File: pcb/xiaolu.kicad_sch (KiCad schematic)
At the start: 35 parts, among them J1 Conn_01x04_Male, J2 AudioJack4, SW1 SW_Push, SW10 SW_Push, SW11 SW_Push, SW12 SW_Push, SW13 SW_Push, SW14 SW_Push, SW15 SW_Push, SW16 SW_Push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

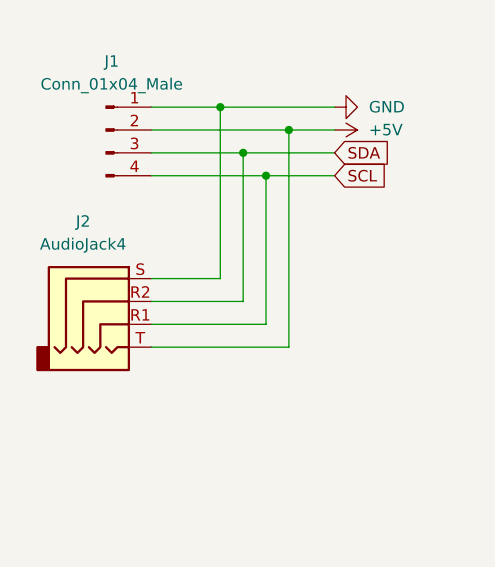
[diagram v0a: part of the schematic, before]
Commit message: fix TRRS symbol
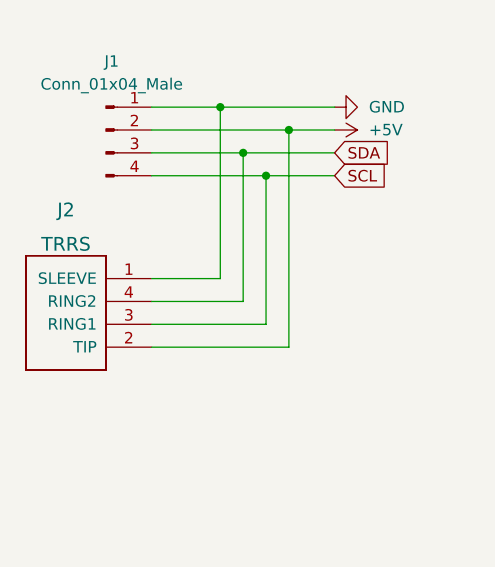
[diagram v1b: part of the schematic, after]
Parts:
- J2: value AudioJack4 -> TRRS; symbol Connector:AudioJack4 -> keebio:TRRS
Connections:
- net +5V: now also J2.2 (TIP); no longer J2.T
- net GND: now also J2.1 (SLEEVE); no longer J2.S
- net SCL: now also J2.3 (RING1); no longer J2.R1
- net SDA: now also J2.4 (RING2); no longer J2.R2
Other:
- moved on the sheet: J2
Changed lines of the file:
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@@
     (pin "1")
   )
-  (symbol (lib_id "Connector:AudioJack4") (at 63.5 132.08 0) (unit 1)
-    (in_bom yes) (on_board yes) (fields_autoplaced)
-    (property "Reference" "J2" (id 0) (at 60.96 123.19 0))
-    (property "Value" "AudioJack4" (id 1) (at 60.96 125.73 0))
-    (property "Footprint" "Xiaolu-Specific:TRRS-PJ-320A" (id 2) (at 63.5 132.08 0)
-      (effects (font (size 1.27 1.27)) hide)
-    )
-    (property "Datasheet" "~" (id 3) (at 63.5 132.08 0)
-      (effects (font (size 1.27 1.27)) hide)
-    )
-    (pin "R1")
-    (pin "R2")
-    (pin "S")
-    (pin "T")
+  (symbol (lib_id "keebio:TRRS") (at 59.69 127 180) (unit 1)
+    (in_bom yes) (on_board yes) (fields_autoplaced)
+    (property "Reference" "J2" (id 0) (at 59.055 121.92 0)
+      (effects (font (size 1.524 1.524)))
+    )
+    (property "Value" "TRRS" (id 1) (at 59.055 125.73 0)
+      (effects (font (size 1.524 1.524)))
+    )
+    (property "Footprint" "Xiaolu-Specific:TRRS-PJ-320A" (id 2) (at 55.88 127 0)
+      (effects (font (size 1.524 1.524)) hide)
+    )
+    (property "Datasheet" "~" (id 3) (at 55.88 127 0)
+      (effects (font (size 1.524 1.524)) hide)
+    )
+    (pin "1")
+    (pin "2")
+    (pin "3")
+    (pin "4")
   )
   (symbol (lib_id "Device:D_Small") (at 236.22 59.69 90) (unit 1)
@@
     )
     (path "/75c6c114-4c92-4cd3-b594-b71491cab033"
-      (reference "J2") (unit 1) (value "AudioJack4") (footprint "Xiaolu-Specific:TRRS-PJ-320A")
+      (reference "J2") (unit 1) (value "TRRS") (footprint "Xiaolu-Specific:TRRS-PJ-320A")
     )
     (path "/a7ae1a4c-2b24-4280-96fc-27eb49b6c4a7"

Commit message: replace XIAO footprint with XIAO-Generic-Hybrid-14P-2.54-21X17.8MM
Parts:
- U1: footprint Xiaolu-Specific:XIAO-SAMD21-RP2040-Hybrid-14P-2.54-21X17.8MM -> Xiaolu-Specific:XIAO-Generic-Hybrid-14P-2.54-21X17.8MM
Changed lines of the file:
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@@
       (effects (font (size 1.27 1.27)) (justify left))
     )
-    (property "Footprint" "Xiaolu-Specific:XIAO-SAMD21-RP2040-Hybrid-14P-2.54-21X17.8MM" (id 2) (at 74.93 49.53 0)
+    (property "Footprint" "Xiaolu-Specific:XIAO-Generic-Hybrid-14P-2.54-21X17.8MM" (id 2) (at 74.93 49.53 0)
       (effects (font (size 1.27 1.27)) hide)
     )
@@
     )
     (path "/31979451-8777-4b8b-b45d-fef92cd05572"
-      (reference "U1") (unit 1) (value "Seeed Studio XIAO SAMD21") (footprint "Xiaolu-Specific:XIAO-SAMD21-RP2040-Hybrid-14P-2.54-21X17.8MM")
-    )
-  )
+      (reference "U1") (unit 1) (value "Seeed Studio XIAO SAMD21") (footprint "Xiaolu-Specific:XIAO-Generic-Hybrid-14P-2.54-21X17.8MM")
+    )
+  )

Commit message: fix Grove connector
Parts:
- J1: footprint Xiaolu-Specific:NS-Tech_Grove_1x04_P2mm_Horizontal -> Connector:NS-Tech_Grove_1x04_P2mm_Vertical
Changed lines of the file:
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@@
     (property "Reference" "J1" (id 0) (at 64.135 105.41 0))
     (property "Value" "Conn_01x04_Male" (id 1) (at 64.135 107.95 0))
-    (property "Footprint" "Xiaolu-Specific:NS-Tech_Grove_1x04_P2mm_Horizontal" (id 2) (at 63.5 113.03 0)
+    (property "Footprint" "Connector:NS-Tech_Grove_1x04_P2mm_Vertical" (id 2) (at 63.5 113.03 0)
       (effects (font (size 1.27 1.27)) hide)
     )
@@
     )
     (path "/b1765cdf-6a38-4dd8-bdad-abffed91abd0"
-      (reference "J1") (unit 1) (value "Conn_01x04_Male") (footprint "Xiaolu-Specific:NS-Tech_Grove_1x04_P2mm_Horizontal")
+      (reference "J1") (unit 1) (value "Conn_01x04_Male") (footprint "Connector:NS-Tech_Grove_1x04_P2mm_Vertical")
     )
     (path "/75c6c114-4c92-4cd3-b594-b71491cab033"

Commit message: use NS-Tech_Grove_1x04_P2mm_Hybrid.kicad_mod for grove connector footprint and fix the Grove connector position
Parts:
- J1: footprint Connector:NS-Tech_Grove_1x04_P2mm_Vertical -> Xiaolu-Specific:NS-Tech_Grove_1x04_P2mm_Hybrid
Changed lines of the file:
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@@
     (property "Reference" "J1" (id 0) (at 64.135 105.41 0))
     (property "Value" "Conn_01x04_Male" (id 1) (at 64.135 107.95 0))
-    (property "Footprint" "Connector:NS-Tech_Grove_1x04_P2mm_Vertical" (id 2) (at 63.5 113.03 0)
+    (property "Footprint" "Xiaolu-Specific:NS-Tech_Grove_1x04_P2mm_Hybrid" (id 2) (at 63.5 113.03 0)
       (effects (font (size 1.27 1.27)) hide)
     )
@@
     )
     (path "/b1765cdf-6a38-4dd8-bdad-abffed91abd0"
-      (reference "J1") (unit 1) (value "Conn_01x04_Male") (footprint "Connector:NS-Tech_Grove_1x04_P2mm_Vertical")
+      (reference "J1") (unit 1) (value "Conn_01x04_Male") (footprint "Xiaolu-Specific:NS-Tech_Grove_1x04_P2mm_Hybrid")
     )
     (path "/75c6c114-4c92-4cd3-b594-b71491cab033"

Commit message: Assign "LCSC Part #" of diodes (D1....D16) to C2128 (1N4148WS)
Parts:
- D1, D11, D12, D14, D2, D3, D5, D7, D8, D9, SW10, SW13, SW14, SW16, SW4, SW8, SW9: LCSC Part # (none) -> C2128
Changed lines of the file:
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@@
+      (effects (font (size 1.27 1.27)) hide)
+    )
+    (property "LCSC Part #" "C2128" (id 4) (at 261.62 85.09 90)
       (effects (font (size 1.27 1.27)) hide)
     )
@@
       (effects (font (size 1.27 1.27)) hide)
     )
+    (property "LCSC Part #" "C2128" (id 4) (at 185.42 85.09 90)
+      (effects (font (size 1.27 1.27)) hide)
+    )
     (pin "1")
     (pin "2")
@@
     )
     (property "Datasheet" "" (id 3) (at 160.02 180.34 0)
+      (effects (font (size 1.27 1.27)) hide)
+    )
+    (property "LCSC Part #" "C2128" (id 4) (at 160.02 180.34 0)
       (effects (font (size 1.27 1.27)) hide)
     )
@@
       (effects (font (size 1.27 1.27)) hide)
     )
+    (property "LCSC Part #" "C2128" (id 4) (at 177.8 120.65 0)
+      (effects (font (size 1.27 1.27)) hide)
+    )
     (pin "1")
     (pin "2")
@@
     )
     (property "Datasheet" "~" (id 3) (at 228.6 44.45 0)
+      (effects (font (size 1.27 1.27)) hide)
+    )
+    (property "LCSC Part #" "C2128" (id 4) (at 228.6 44.45 0)
       (effects (font (size 1.27 1.27)) hide)
     )
@@
       (effects (font (size 1.27 1.27)) hide)
     )
+    (property "LCSC Part #" "C2128" (id 4) (at 210.82 135.89 90)
+      (effects (font (size 1.27 1.27)) hide)
+    )
     (pin "1")
     (pin "2")
@@
       (effects (font (size 1.27 1.27)) hide)
     )
+    (property "LCSC Part #" "C2128" (id 4) (at 160.02 187.96 0)
+      (effects (font (size 1.27 1.27)) hide)
+    )
     (pin "1")
   )
@@
       (effects (font (size 1.27 1.27)) hide)
     )
+    (property "LCSC Part #" "C2128" (id 4) (at 236.22 110.49 90)
+      (effects (font (size 1.27 1.27)) hide)
+    )
     (pin "1")
     (pin "2")
@@
     )
     (property "Datasheet" "" (id 3) (at 160.02 172.72 0)
+      (effects (font (size 1.27 1.27)) hide)
+    )
+    (property "LCSC Part #" "C2128" (id 4) (at 160.02 172.72 0)
       (effects (font (size 1.27 1.27)) hide)
     )
@@
       (effects (font (size 1.27 1.27)) hide)
     )
+    (property "LCSC Part #" "C2128" (id 4) (at 160.02 172.72 0)
+      (effects (font (size 1.27 1.27)) hide)
+    )
     (pin "1")
   )
@@
     )
     (property "Datasheet" "~" (id 3) (at 236.22 59.69 90)
+      (effects (font (size 1.27 1.27)) hide)
+    )
+    (property "LCSC Part #" "C2128" (id 4) (at 236.22 59.69 90)
       (effects (font (size 1.27 1.27)) hide)
     )
@@
       (effects (font (size 1.27 1.27)) hide)
     )
+    (property "LCSC Part #" "C2128" (id 4) (at 254 44.45 0)
+      (effects (font (size 1.27 1.27)) hide)
+    )
     (pin "1")
     (pin "2")
@@
     )
     (property "Datasheet" "" (id 3) (at 86.36 76.2 0)
+      (effects (font (size 1.27 1.27)) hide)
+    )
+    (property "LCSC Part #" "C2128" (id 4) (at 86.36 76.2 0)
       (effects (font (size 1.27 1.27)) hide)
     )
@@
       (effects (font (size 1.27 1.27)) hide)
     )
+    (property "LCSC Part #" "C2128" (id 4) (at 254 120.65 0)
+      (effects (font (size 1.27 1.27)) hide)
+    )
     (pin "1")
     (pin "2")
@@
       (effects (font (size 1.27 1.27)) hide)
     )
+    (property "LCSC Part #" "C2128" (id 4) (at 203.2 120.65 0)
+      (effects (font (size 1.27 1.27)) hide)
+    )
     (pin "1")
     (pin "2")
@@
       (effects (font (size 1.27 1.27)) hide)
     )
+    (property "LCSC Part #" "C2128" (id 4) (at 210.82 110.49 90)
+      (effects (font (size 1.27 1.27)) hide)
+    )
     (pin "1")
     (pin "2")
@@
       (effects (font (size 1.27 1.27)) hide)
     )
+    (property "LCSC Part #" "C2128" (id 4) (at 185.42 59.69 90)
+      (effects (font (size 1.27 1.27)) hide)
+    )
     (pin "1")
     (pin "2")
@@
     )
     (property "Datasheet" "~" (id 3) (at 210.82 59.69 90)
+      (effects (font (size 1.27 1.27)) hide)
+    )
+    (property "LCSC Part #" "C2128" (id 4) (at 210.82 59.69 90)
       (effects (font (size 1.27 1.27)) hide)
     )
@@
       (effects (font (size 1.27 1.27)) hide)
     )
+    (property "LCSC Part #" "C2128" (id 4) (at 254 69.85 0)
+      (effects (font (size 1.27 1.27)) hide)
+    )
     (pin "1")
     (pin "2")
@@
     )
     (property "Datasheet" "" (id 3) (at 88.9 113.03 0)
+      (effects (font (size 1.27 1.27)) hide)
+    )
+    (property "LCSC Part #" "C2128" (id 4) (at 88.9 113.03 0)
       (effects (font (size 1.27 1.27)) hide)
     )
@@
       (effects (font (size 1.27 1.27)) hide)
     )
+    (property "LCSC Part #" "C2128" (id 4) (at 185.42 110.49 90)
+      (effects (font (size 1.27 1.27)) hide)
+    )
     (pin "1")
     (pin "2")
@@
       (effects (font (size 1.27 1.27)) hide)
     )
+    (property "LCSC Part #" "C2128" (id 4) (at 236.22 135.89 90)
+      (effects (font (size 1.27 1.27)) hide)
+    )
     (pin "1")
     (pin "2")
@@
       (effects (font (size 1.27 1.27)) hide)
     )
+    (property "LCSC Part #" "C2128" (id 4) (at 228.6 69.85 0)
+      (effects (font (size 1.27 1.27)) hide)
+    )

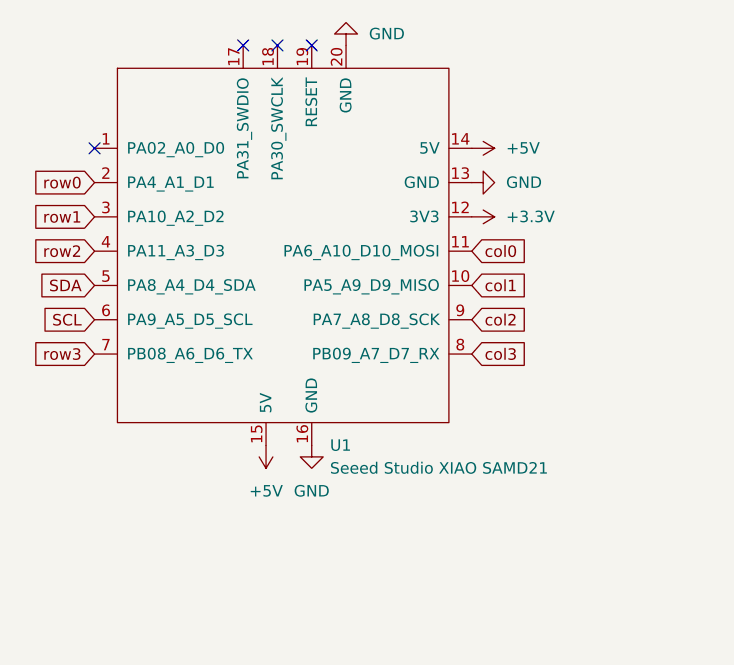
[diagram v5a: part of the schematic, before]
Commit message: flag unconnected to unused pads of xiao
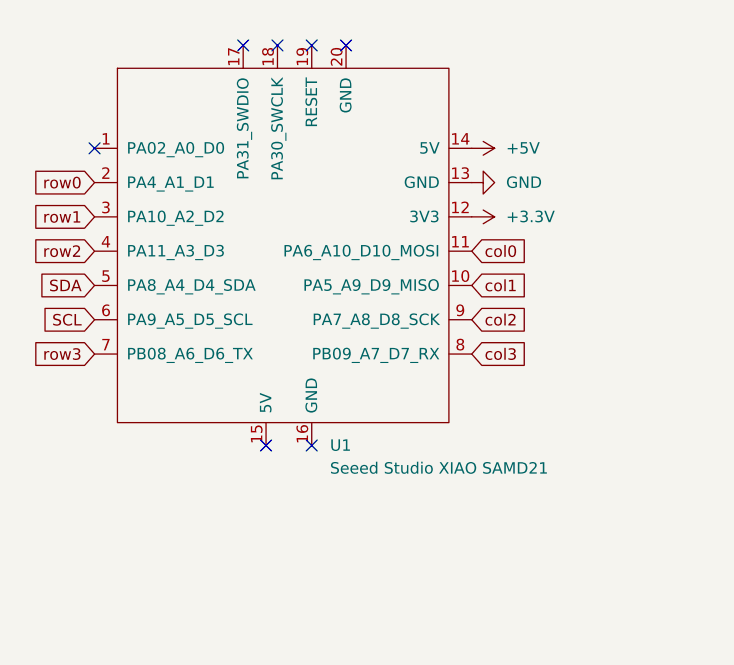
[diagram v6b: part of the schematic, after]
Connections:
- net +5V: no longer U1.15 (5V)
- net GND: no longer U1.16 (GND), U1.20 (GND)
- no-connect marks 4 -> 7
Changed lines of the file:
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@@
   (no_connect (at 78.74 31.75))
   (no_connect (at 86.36 31.75))
+  (no_connect (at 81.28 76.2))
+  (no_connect (at 86.36 76.2))
   (no_connect (at 62.23 43.18))
   (no_connect (at 82.55 31.75))
+  (no_connect (at 90.17 31.75))
   (wire (pts (xy 236.22 125.73) (xy 233.68 125.73))
     (stroke (width 0) (type default) (color 0 0 0 0))
@@
     )
     (property "Datasheet" "" (id 3) (at 104.14 43.18 0)
-      (effects (font (size 1.27 1.27)) hide)
-    )
-    (pin "1")
-  )
-  (symbol (lib_id "power:GND") (at 90.17 31.75 180) (unit 1)
-    (in_bom yes) (on_board yes) (fields_autoplaced)
-    (property "Reference" "#PWR05" (id 0) (at 90.17 25.4 0)
-      (effects (font (size 1.27 1.27)) hide)
-    )
-    (property "Value" "GND" (id 1) (at 92.71 30.4799 0)
-      (effects (font (size 1.27 1.27)) (justify right))
-    )
-    (property "Footprint" "" (id 2) (at 90.17 31.75 0)
-      (effects (font (size 1.27 1.27)) hide)
-    )
-    (property "Datasheet" "" (id 3) (at 90.17 31.75 0)
       (effects (font (size 1.27 1.27)) hide)
     )
@@
     (pin "2")
   )
-  (symbol (lib_id "power:+5V") (at 81.28 76.2 180) (unit 1)
-    (in_bom yes) (on_board yes) (fields_autoplaced)
-    (property "Reference" "#PWR03" (id 0) (at 81.28 72.39 0)
-      (effects (font (size 1.27 1.27)) hide)
-    )
-    (property "Value" "+5V" (id 1) (at 81.28 81.28 0))
-    (property "Footprint" "" (id 2) (at 81.28 76.2 0)
-      (effects (font (size 1.27 1.27)) hide)
-    )
-    (property "Datasheet" "" (id 3) (at 81.28 76.2 0)
-      (effects (font (size 1.27 1.27)) hide)
-    )
-    (pin "1")
-  )
   (symbol (lib_id "power:+3.3V") (at 160.02 187.96 270) (unit 1)
     (in_bom yes) (on_board yes) (fields_autoplaced)
@@
     (pin "2")
   )
-  (symbol (lib_id "power:GND") (at 86.36 76.2 0) (unit 1)
-    (in_bom yes) (on_board yes) (fields_autoplaced)
-    (property "Reference" "#PWR04" (id 0) (at 86.36 82.55 0)
-      (effects (font (size 1.27 1.27)) hide)
-    )
-    (property "Value" "GND" (id 1) (at 86.36 81.28 0))
-    (property "Footprint" "" (id 2) (at 86.36 76.2 0)
-      (effects (font (size 1.27 1.27)) hide)
-    )
-    (property "Datasheet" "" (id 3) (at 86.36 76.2 0)
-      (effects (font (size 1.27 1.27)) hide)
-    )
-    (property "LCSC Part #" "C2128" (id 4) (at 86.36 76.2 0)
-      (effects (font (size 1.27 1.27)) hide)
-    )
-    (pin "1")
-  )
   (symbol (lib_id "power:PWR_FLAG") (at 160.02 180.34 90) (unit 1)
     (in_bom yes) (on_board yes) (fields_autoplaced)
@@
       (reference "#PWR02") (unit 1) (value "+5V") (footprint "")
     )
-    (path "/3553bc35-9f95-4817-85a7-17e531db1a71"
-      (reference "#PWR03") (unit 1) (value "+5V") (footprint "")
-    )
-    (path "/8adb19c1-6f4e-4373-9001-846d6097e7f5"
-      (reference "#PWR04") (unit 1) (value "GND") (footprint "")
-    )
-    (path "/0cd8ac2f-d4e5-49d7-95f0-562595e83db6"
-      (reference "#PWR05") (unit 1) (value "GND") (footprint "")
-    )
     (path "/0b31afd7-5fe7-4ed2-8f8a-50ac88bd6e7e"

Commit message: fix "LCSC Part #"
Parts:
- D10, D13, D15, D16, D4, D6: LCSC Part # (none) -> C2128
- SW10, SW13, SW14, SW16, SW4, SW8, SW9: LCSC Part # C2128 -> (none)
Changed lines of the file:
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@@
       (effects (font (size 1.27 1.27)) hide)
     )
-    (property "LCSC Part #" "C2128" (id 4) (at 261.62 85.09 90)
+    (property "LCSC Part #" "C2128" (id 3) (at 261.62 85.09 90)
       (effects (font (size 1.27 1.27)) hide)
     )
@@
       (effects (font (size 1.27 1.27)) hide)
     )
+    (property "LCSC Part #" "C2128" (id 3) (at 185.42 135.89 90)
+      (effects (font (size 1.27 1.27)) hide)
+    )
     (pin "1")
     (pin "2")
@@
       (effects (font (size 1.27 1.27)) hide)
     )
-    (property "LCSC Part #" "C2128" (id 4) (at 185.42 85.09 90)
+    (property "LCSC Part #" "C2128" (id 3) (at 185.42 85.09 90)
       (effects (font (size 1.27 1.27)) hide)
     )
@@
       (effects (font (size 1.27 1.27)) hide)
     )
+    (property "LCSC Part #" "C2128" (id 3) (at 210.82 85.09 90)
+      (effects (font (size 1.27 1.27)) hide)
+    )
     (pin "1")
     (pin "2")
@@
     )
     (property "Datasheet" "" (id 3) (at 160.02 180.34 0)
-      (effects (font (size 1.27 1.27)) hide)
-    )
-    (property "LCSC Part #" "C2128" (id 4) (at 160.02 180.34 0)
       (effects (font (size 1.27 1.27)) hide)
     )
@@
       (effects (font (size 1.27 1.27)) hide)
     )
-    (property "LCSC Part #" "C2128" (id 4) (at 177.8 120.65 0)
-      (effects (font (size 1.27 1.27)) hide)
-    )
     (pin "1")
     (pin "2")
@@
     )
     (property "Datasheet" "~" (id 3) (at 261.62 59.69 90)
+      (effects (font (size 1.27 1.27)) hide)
+    )
+    (property "LCSC Part #" "C2128" (id 3) (at 261.62 59.69 90)
       (effects (font (size 1.27 1.27)) hide)
     )
@@
     )
     (property "Datasheet" "~" (id 3) (at 228.6 44.45 0)
-      (effects (font (size 1.27 1.27)) hide)
-    )
-    (property "LCSC Part #" "C2128" (id 4) (at 228.6 44.45 0)
       (effects (font (size 1.27 1.27)) hide)
     )
@@
       (effects (font (size 1.27 1.27)) hide)
     )
-    (property "LCSC Part #" "C2128" (id 4) (at 210.82 135.89 90)
+    (property "LCSC Part #" "C2128" (id 3) (at 210.82 135.89 90)
       (effects (font (size 1.27 1.27)) hide)
     )
@@
       (effects (font (size 1.27 1.27)) hide)
     )
-    (property "LCSC Part #" "C2128" (id 4) (at 160.02 187.96 0)
-      (effects (font (size 1.27 1.27)) hide)
-    )
     (pin "1")
   )
@@
       (effects (font (size 1.27 1.27)) hide)
     )
-    (property "LCSC Part #" "C2128" (id 4) (at 236.22 110.49 90)
+    (property "LCSC Part #" "C2128" (id 3) (at 236.22 110.49 90)
       (effects (font (size 1.27 1.27)) hide)
     )
@@
       (effects (font (size 1.27 1.27)) hide)
     )
+    (property "LCSC Part #" "C2128" (id 3) (at 261.62 110.49 90)
+      (effects (font (size 1.27 1.27)) hide)
+    )
     (pin "1")
     (pin "2")
@@
     )
     (property "Datasheet" "" (id 3) (at 160.02 172.72 0)
-      (effects (font (size 1.27 1.27)) hide)
-    )
-    (property "LCSC Part #" "C2128" (id 4) (at 160.02 172.72 0)
       (effects (font (size 1.27 1.27)) hide)
     )
@@
       (effects (font (size 1.27 1.27)) hide)
     )
-    (property "LCSC Part #" "C2128" (id 4) (at 160.02 172.72 0)
-      (effects (font (size 1.27 1.27)) hide)
-    )
     (pin "1")
   )
@@
       (effects (font (size 1.27 1.27)) hide)
     )
-    (property "LCSC Part #" "C2128" (id 4) (at 236.22 59.69 90)
+    (property "LCSC Part #" "C2128" (id 3) (at 236.22 59.69 90)
       (effects (font (size 1.27 1.27)) hide)
     )
@@
       (effects (font (size 1.27 1.27)) hide)
     )
-    (property "LCSC Part #" "C2128" (id 4) (at 254 44.45 0)
-      (effects (font (size 1.27 1.27)) hide)
-    )
     (pin "1")
     (pin "2")
@@
     )
     (property "Datasheet" "~" (id 3) (at 261.62 135.89 90)
+      (effects (font (size 1.27 1.27)) hide)
+    )
+    (property "LCSC Part #" "C2128" (id 3) (at 261.62 135.89 90)
       (effects (font (size 1.27 1.27)) hide)
     )
@@
       (effects (font (size 1.27 1.27)) hide)
     )
-    (property "LCSC Part #" "C2128" (id 4) (at 254 120.65 0)
-      (effects (font (size 1.27 1.27)) hide)
-    )
     (pin "1")
     (pin "2")
@@
       (effects (font (size 1.27 1.27)) hide)
     )
-    (property "LCSC Part #" "C2128" (id 4) (at 203.2 120.65 0)
-      (effects (font (size 1.27 1.27)) hide)
-    )
     (pin "1")
     (pin "2")
@@
       (effects (font (size 1.27 1.27)) hide)
     )
-    (property "LCSC Part #" "C2128" (id 4) (at 210.82 110.49 90)
+    (property "LCSC Part #" "C2128" (id 3) (at 210.82 110.49 90)
       (effects (font (size 1.27 1.27)) hide)
     )
@@
       (effects (font (size 1.27 1.27)) hide)
     )
-    (property "LCSC Part #" "C2128" (id 4) (at 185.42 59.69 90)
+    (property "LCSC Part #" "C2128" (id 3) (at 185.42 59.69 90)
       (effects (font (size 1.27 1.27)) hide)
     )
@@
       (effects (font (size 1.27 1.27)) hide)
     )
-    (property "LCSC Part #" "C2128" (id 4) (at 210.82 59.69 90)
+    (property "LCSC Part #" "C2128" (id 3) (at 210.82 59.69 90)
       (effects (font (size 1.27 1.27)) hide)
     )
@@
       (effects (font (size 1.27 1.27)) hide)
     )
-    (property "LCSC Part #" "C2128" (id 4) (at 254 69.85 0)
-      (effects (font (size 1.27 1.27)) hide)
-    )
     (pin "1")
     (pin "2")
@@
       (effects (font (size 1.27 1.27)) hide)
     )
+    (property "LCSC Part #" "C2128" (id 3) (at 236.22 85.09 90)
+      (effects (font (size 1.27 1.27)) hide)
+    )
     (pin "1")
     (pin "2")
@@
     )
     (property "Datasheet" "" (id 3) (at 88.9 113.03 0)
-      (effects (font (size 1.27 1.27)) hide)
-    )
-    (property "LCSC Part #" "C2128" (id 4) (at 88.9 113.03 0)
       (effects (font (size 1.27 1.27)) hide)
     )
@@
       (effects (font (size 1.27 1.27)) hide)
     )
-    (property "LCSC Part #" "C2128" (id 4) (at 185.42 110.49 90)
+    (property "LCSC Part #" "C2128" (id 3) (at 185.42 110.49 90)
       (effects (font (size 1.27 1.27)) hide)
     )
@@
       (effects (font (size 1.27 1.27)) hide)
     )
-    (property "LCSC Part #" "C2128" (id 4) (at 236.22 135.89 90)
+    (property "LCSC Part #" "C2128" (id 3) (at 236.22 135.89 90)
       (effects (font (size 1.27 1.27)) hide)
     )
@@
       (effects (font (size 1.27 1.27)) hide)
     )
-    (property "LCSC Part #" "C2128" (id 4) (at 228.6 69.85 0)
-      (effects (font (size 1.27 1.27)) hide)
-    )
